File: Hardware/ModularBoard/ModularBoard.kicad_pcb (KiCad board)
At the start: 2 copper layers, 25.4 x 68.6 mm, 16 parts, among them IC1 WS2811-5050, IC2 WS2811-5050, IC3 WS2811-5050, IC4 WS2811-5050, IC5 ATTINY85-P, J1 GSG-USB-MICRO-B, K1 CONN_3, K2 CONN_3, K3 CONN_3, K4 CONN_3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

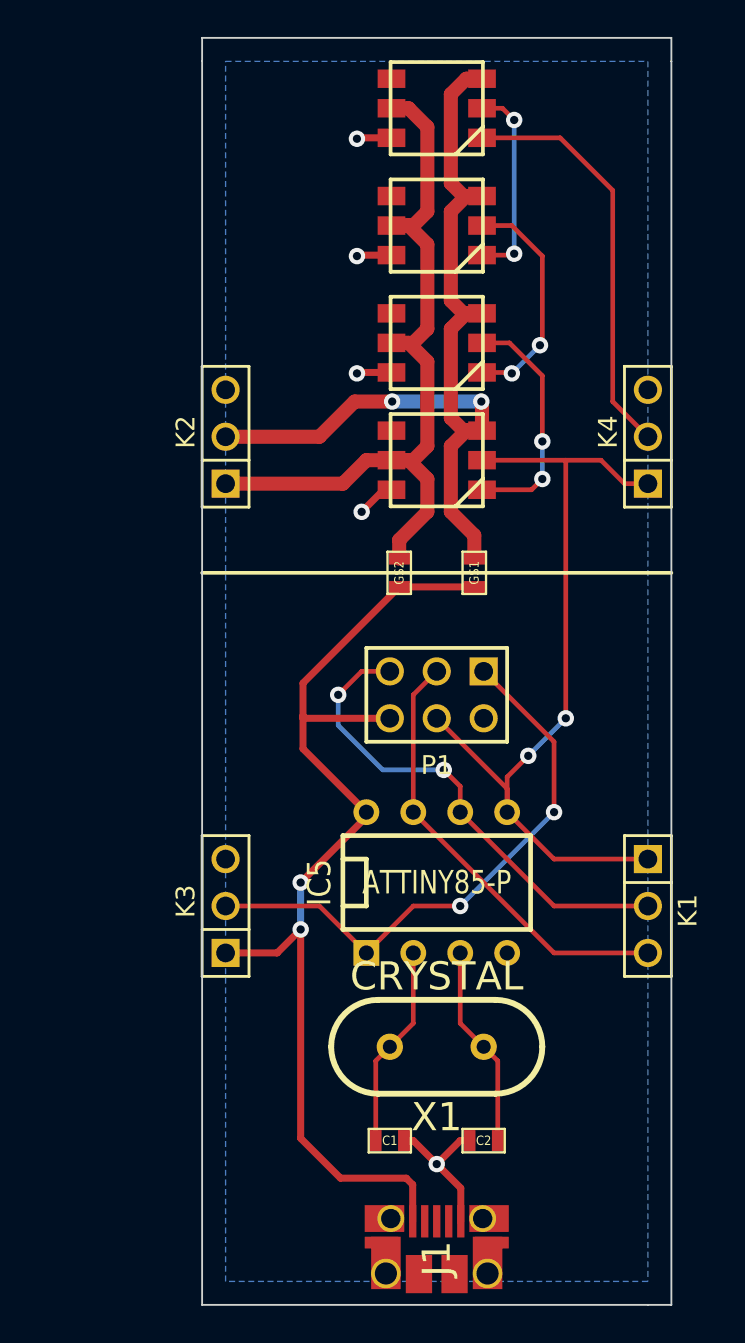
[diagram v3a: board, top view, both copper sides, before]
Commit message: Made the board more compact, might do more by putting ICSP and USB side by side
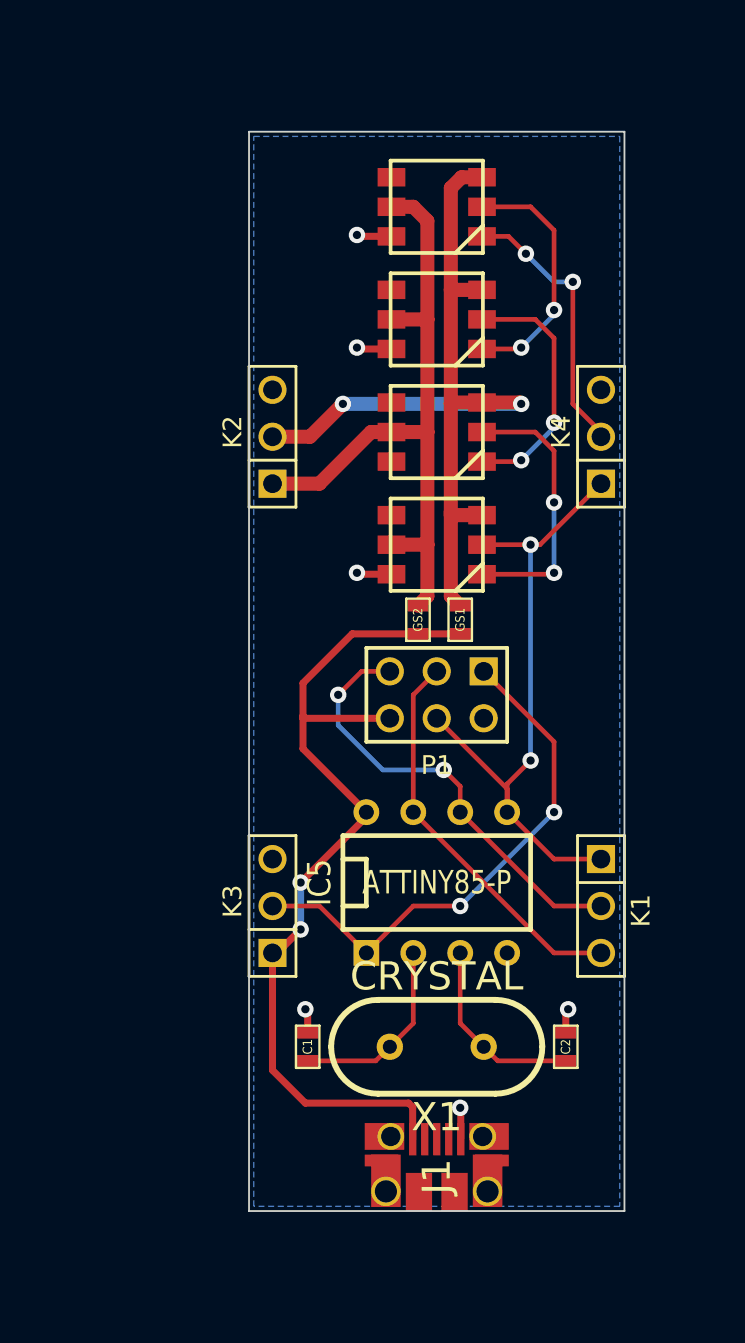
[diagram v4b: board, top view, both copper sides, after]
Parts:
- moved C1 6.75 mm to (219.1, 158.8), turned to 90 degrees
- moved C2 6.75 mm to (233.0, 158.8), turned to 90 degrees
- moved IC4 5.33 mm to (226.1, 113.3)
- moved IC3 5.08 mm to (226.1, 119.4)
- moved IC2 4.83 mm to (226.1, 125.5)
- moved IC1 4.57 mm to (226.1, 131.6)
- moved J1 4.44 mm to (226.1, 168.3)
- moved GS2 2.74 mm to (225.0, 135.6)
- moved GS1 2.65 mm to (227.3, 135.6)
- moved K1 2.54 mm to (234.9, 151.1)
- moved K4 2.54 mm to (234.9, 125.7)
- moved K2 2.54 mm to (217.2, 125.7)
- moved K3 2.54 mm to (217.2, 151.1)
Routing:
- net /MOSI: track 45.2 -> 35.6 mm
- net +5V: track 57.5 -> 49.0 mm
- net VDD: track 44.4 -> 36.7 mm
- net /DO: track 22.4 -> 14.9 mm, vias 0 -> 2
- net GND: track 16.0 -> 10.1 mm, vias 5 -> 6
- net VCC: track 51.4 -> 46.4 mm
- net N-0000013: track 11.0 -> 13.7 mm
- net /MISO: track 26.6 -> 24.1 mm
- net /SCK: track 24.0 -> 21.5 mm
- net /RESET: track 31.2 -> 28.6 mm
- net N-000002: track 13.1 -> 14.9 mm
- net N-0000012: track 12.6 -> 13.8 mm
- net N-0000018: track 11.0 -> 10.4 mm
- net N-0000017: track 11.0 -> 10.4 mm
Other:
- board size 25.4 x 68.6 mm -> 20.3 x 58.4 mm

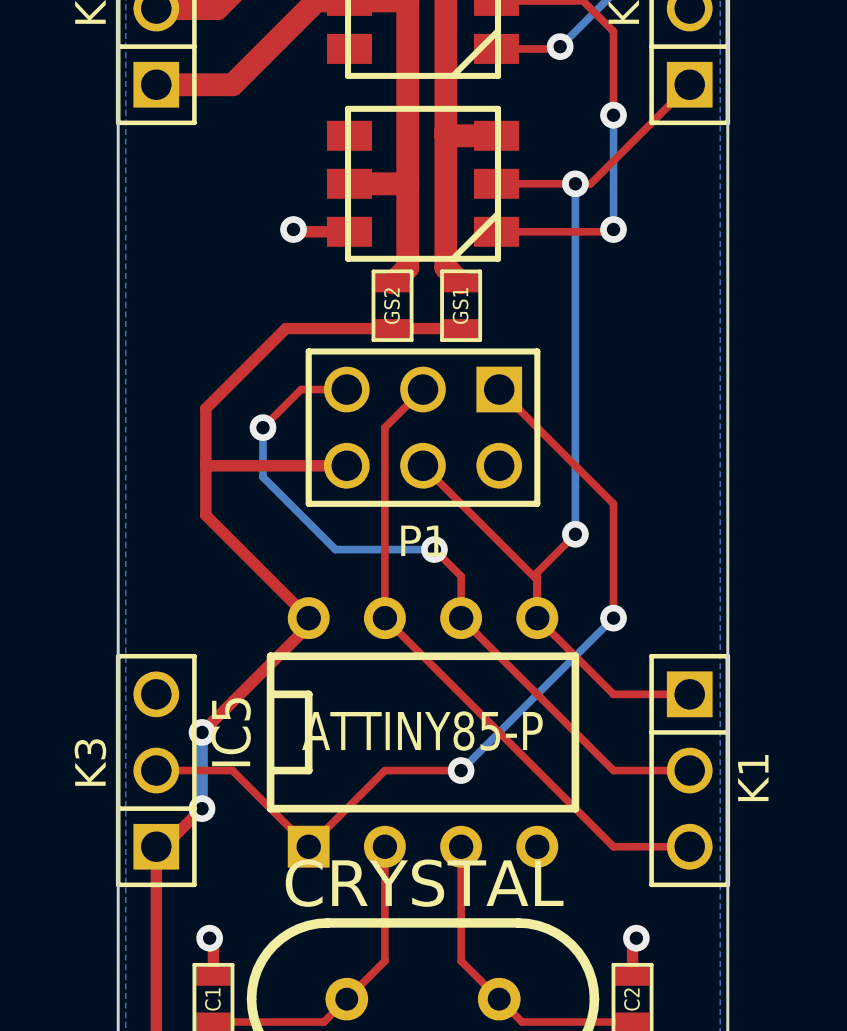
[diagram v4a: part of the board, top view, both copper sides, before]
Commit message: Fixed ICSP header
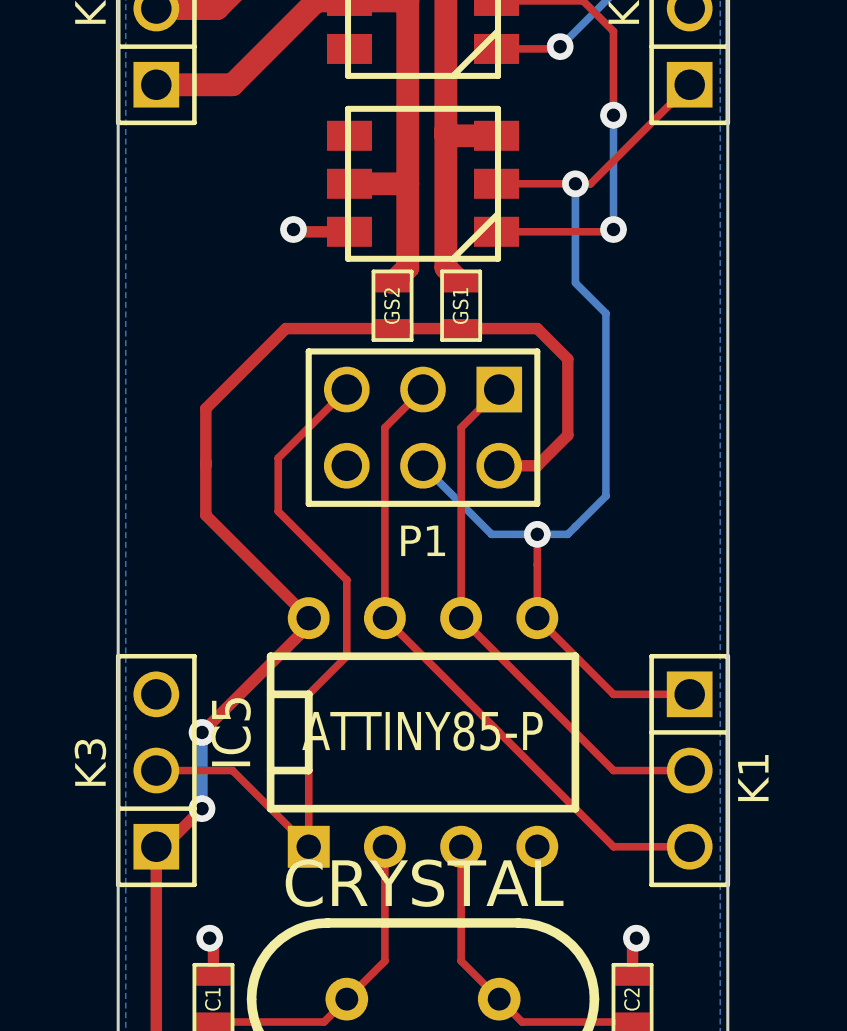
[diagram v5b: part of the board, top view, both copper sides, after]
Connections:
- P1 pad 1: /RESET -> /MISO
- P1 pad 2: GND -> +5V
- P1 pad 5: /MISO -> /RESET
- P1 pad 6: +5V -> GND
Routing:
- net /MISO: track 24.1 -> 17.9 mm, vias 2 -> 0
- net /RESET: track 28.6 -> 23.8 mm, vias 2 -> 0
- net +5V: track 49.0 -> 53.5 mm

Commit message: Its compact! Fits in 5x5cm square
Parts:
- moved P1 25.6 mm to (232.9, 164.3)
- moved K4 15.5 mm to (237.5, 141.0)
- moved K2 15.2 mm to (217.2, 141.0)
- moved GS1 10.5 mm to (228.6, 146.1)
- moved GS2 10.5 mm to (226.3, 146.1)
- moved IC1 9.99 mm to (227.3, 141.5)
- moved IC2 9.99 mm to (227.3, 135.4)
- moved IC3 9.99 mm to (227.3, 129.3)
- moved IC4 9.99 mm to (227.3, 123.2)
- moved C2 9.37 mm to (224.0, 161.3), turned to 0 degrees
- moved C1 7.67 mm to (218.2, 151.1), turned to 180 degrees
- moved IC5 7.58 mm to (230.9, 155.7), turned to 270 degrees
- moved K1 5.68 mm to (237.5, 156.2)
- moved X1 5.49 mm to (223.0, 154.2), turned to 90 degrees
- moved K3 5.08 mm to (217.2, 156.2)
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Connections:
- K1 pad 1: /MOSI -> /SCK
- K1 pad 3: /SCK -> /MOSI
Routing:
- net GND: track 10.1 -> 23.4 mm, vias 6 -> 4
- net /RESET: track 23.8 -> 32.5 mm, vias 0 -> 1
- net /SCK: track 21.5 -> 13.3 mm
- net /MISO: track 17.9 -> 10.9 mm, vias 0 -> 1
- net /MOSI: track 35.1 -> 40.9 mm, vias 2 -> 0
- net /DO: track 14.9 -> 20.1 mm
- net +5V: track 53.5 -> 56.5 mm, vias 2 -> 3
- net N-0000018: track 10.4 -> 8.85 mm
- net N-000005: track 14.9 -> 13.8 mm
- net VCC: track 46.4 -> 47.5 mm
- net N-0000017: track 10.4 -> 9.50 mm
- net VDD: track 36.7 -> 37.5 mm
- net N-0000011: track 13.8 -> 13.2 mm
- net N-0000012: track 13.7 -> 13.2 mm
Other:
- board size 20.3 x 58.4 mm -> 22.9 x 48.3 mm

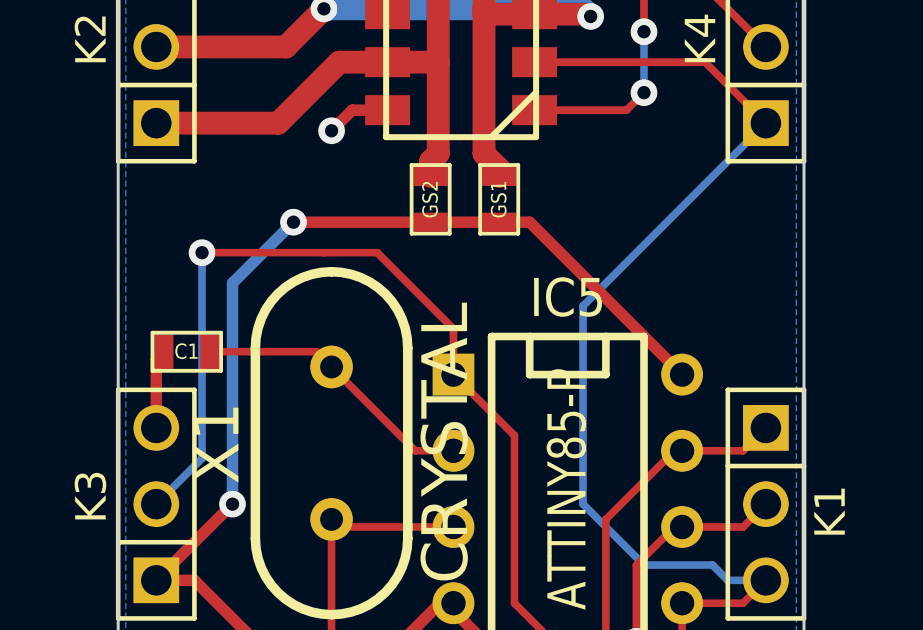
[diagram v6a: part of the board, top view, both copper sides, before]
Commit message: made sure ground was all connected
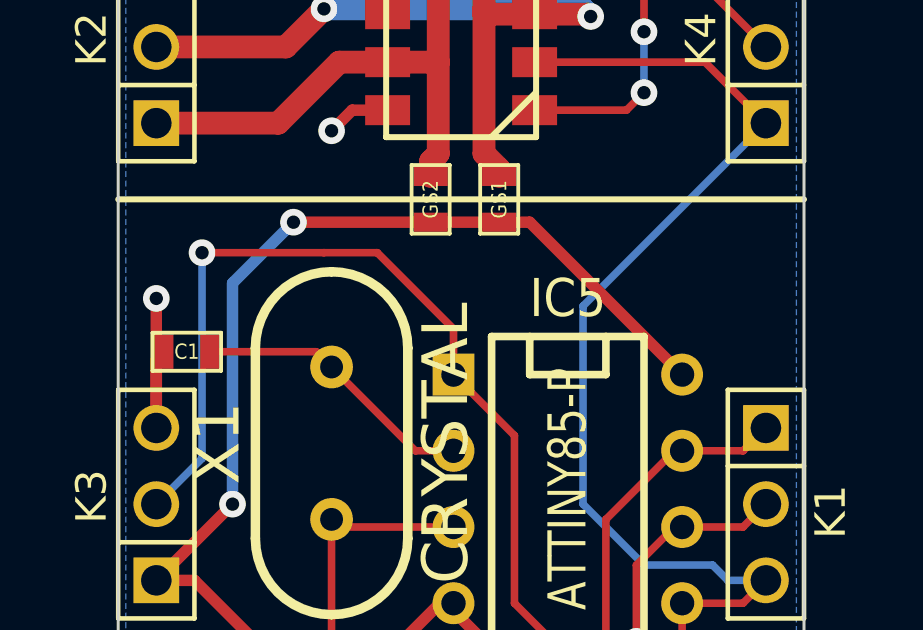
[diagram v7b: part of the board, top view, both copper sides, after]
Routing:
- net GND: track 23.4 -> 27.7 mm, vias 4 -> 5
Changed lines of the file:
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@@
   (general
     (links 43)
-    (no_connects 6)
+    (no_connects 0)
     (area 214.1728 107.42929 237.9472 178.88204)
     (thickness 1.6)
     (drawings 5)
-    (tracks 157)
+    (tracks 159)
     (zones 0)
     (modules 16)
@@
     )
   )
+  (gr_line (start 238.76 146.05) (end 215.9 146.05) (angle 90) (layer F.SilkS) (width 0.2))
   (gr_line (start 215.9 167.64) (end 215.9 119.38) (angle 90) (layer Edge.Cuts) (width 0.1))
   (gr_line (start 238.76 119.38) (end 238.76 167.64) (angle 90) (layer Edge.Cuts) (width 0.1))
   (gr_line (start 215.9 119.38) (end 238.76 119.38) (angle 90) (layer Edge.Cuts) (width 0.1))
   (gr_line (start 238.76 167.64) (end 215.9 167.64) (angle 90) (layer Edge.Cuts) (width 0.1))
-  (dimension 49.784 (width 0.3) (layer F.SilkS)
-    (gr_text "49.784 mm" (at 247.222 142.748 90) (layer F.SilkS)
-      (effects (font (size 1.5 1.5) (thickness 0.3)))
-    )
-    (feature1 (pts (xy 239.522 117.856) (xy 248.572 117.856)))
-    (feature2 (pts (xy 239.522 167.64) (xy 248.572 167.64)))
-    (crossbar (pts (xy 245.872 167.64) (xy 245.872 117.856)))
-    (arrow1a (pts (xy 245.872 117.856) (xy 246.45842 118.982503)))
-    (arrow1b (pts (xy 245.872 117.856) (xy 245.28558 118.982503)))
-    (arrow2a (pts (xy 245.872 167.64) (xy 246.45842 166.513497)))
-    (arrow2b (pts (xy 245.872 167.64) (xy 245.28558 166.513497)))
-  )
   (segment (start 228.6 146.812) (end 229.616 146.812) (width 0.381) (layer F.Cu) (net 1))
   (segment (start 229.616 146.812) (end 234.696 151.892) (width 0.381) (layer F.Cu) (net 1))
@@
   (segment (start 222.21952 162.52952) (end 220.98 161.29) (width 0.381) (layer F.Cu) (net 1))
   (segment (start 220.98 161.29) (end 218.44 158.75) (width 0.381) (layer F.Cu) (net 1))
-  (segment (start 229.78 124.79) (end 230.962 124.79) (width 0.254) (layer F.Cu) (net 2) (status 400000))
-  (segment (start 234.95 138.43) (end 237.49 140.97) (width 0.254) (layer F.Cu) (net 2) (status 800000))
+  (segment (start 229.78 124.79) (end 230.962 124.79) (width 0.254) (layer F.Cu) (net 2))
+  (segment (start 234.95 138.43) (end 237.49 140.97) (width 0.254) (layer F.Cu) (net 2))
   (segment (start 234.95 131.572) (end 234.95 138.43) (width 0.254) (layer F.Cu) (net 2))
   (segment (start 234.95 128.778) (end 234.95 131.572) (width 0.254) (layer F.Cu) (net 2))
@@
   (segment (start 234.696 156.972) (end 236.728 156.972) (width 0.254) (layer F.Cu) (net 3))
   (segment (start 236.728 156.972) (end 237.49 156.21) (width 0.254) (layer F.Cu) (net 3))
-  (segment (start 229.78 141.478) (end 235.458 141.478) (width 0.254) (layer F.Cu) (net 4) (status 400000))
-  (segment (start 235.458 141.478) (end 237.49 143.51) (width 0.254) (layer F.Cu) (net 4) (status 800000))
-  (segment (start 237.49 158.75) (end 236.22 158.75) (width 0.254) (layer B.Cu) (net 4) (status 400000))
-  (segment (start 231.394 149.606) (end 237.49 143.51) (width 0.254) (layer B.Cu) (net 4) (status 800000))
+  (segment (start 229.78 141.478) (end 235.458 141.478) (width 0.254) (layer F.Cu) (net 4))
+  (segment (start 235.458 141.478) (end 237.49 143.51) (width 0.254) (layer F.Cu) (net 4))
+  (segment (start 237.49 158.75) (end 236.22 158.75) (width 0.254) (layer B.Cu) (net 4))
+  (segment (start 231.394 149.606) (end 237.49 143.51) (width 0.254) (layer B.Cu) (net 4))
   (segment (start 231.394 156.21) (end 231.394 149.606) (width 0.254) (layer B.Cu) (net 4))
   (segment (start 233.426 158.242) (end 231.394 156.21) (width 0.254) (layer B.Cu) (net 4))
@@
   (segment (start 234.696 154.432) (end 236.728 154.432) (width 0.254) (layer F.Cu) (net 6))
   (segment (start 236.728 154.432) (end 237.49 153.67) (width 0.254) (layer F.Cu) (net 6))
-  (segment (start 224.88 124.79) (end 223.19 124.79) (width 0.381) (layer F.Cu) (net 7) (status 400000))
+  (segment (start 217.17 153.67) (end 217.17 149.352) (width 0.381) (layer F.Cu) (net 7) (status 400000))
+  (via (at 217.17 149.352) (size 0.889) (layers F.Cu B.Cu) (net 7))
+  (segment (start 224.88 124.79) (end 223.19 124.79) (width 0.381) (layer F.Cu) (net 7))
   (via (at 223.012 124.968) (size 0.889) (layers F.Cu B.Cu) (net 7))
   (segment (start 223.19 124.79) (end 223.012 124.968) (width 0.381) (layer F.Cu) (net 7))
-  (segment (start 224.88 130.886) (end 223.19 130.886) (width 0.381) (layer F.Cu) (net 7) (status 400000))
+  (segment (start 224.88 130.886) (end 223.19 130.886) (width 0.381) (layer F.Cu) (net 7))
   (via (at 223.012 131.064) (size 0.889) (layers F.Cu B.Cu) (net 7))
   (segment (start 223.19 130.886) (end 223.012 131.064) (width 0.381) (layer F.Cu) (net 7))
-  (segment (start 224.88 136.982) (end 223.19 136.982) (width 0.381) (layer F.Cu) (net 7) (status 400000))
+  (segment (start 224.88 136.982) (end 223.19 136.982) (width 0.381) (layer F.Cu) (net 7))
   (via (at 223.012 137.16) (size 0.889) (layers F.Cu B.Cu) (net 7))
   (segment (start 223.19 136.982) (end 223.012 137.16) (width 0.381) (layer F.Cu) (net 7))
-  (segment (start 224.88 143.078) (end 223.698 143.078) (width 0.381) (layer F.Cu) (net 7) (status 400000))
+  (segment (start 224.88 143.078) (end 223.698 143.078) (width 0.381) (layer F.Cu) (net 7))
   (via (at 223.012 143.764) (size 0.889) (layers F.Cu B.Cu) (net 7))
   (segment (start 223.698 143.078) (end 223.012 143.764) (width 0.381) (layer F.Cu) (net 7))
@@
   (segment (start 231.902 136.906) (end 233.426 135.382) (width 0.254) (layer B.Cu) (net 8))
   (via (at 233.426 135.382) (size 0.889) (layers F.Cu B.Cu) (net 8))
-  (segment (start 229.78 129.286) (end 231.902 129.286) (width 0.254) (layer F.Cu) (net 8) (status 400000))
-  (segment (start 231.826 136.982) (end 229.78 136.982) (width 0.254) (layer F.Cu) (net 8) (status 800000))
+  (segment (start 229.78 129.286) (end 231.902 129.286) (width 0.254) (layer F.Cu) (net 8))
+  (segment (start 231.826 136.982) (end 229.78 136.982) (width 0.254) (layer F.Cu) (net 8))
   (segment (start 233.426 130.81) (end 231.902 129.286) (width 0.254) (layer F.Cu) (net 8))
   (segment (start 233.426 129.286) (end 233.426 124.714) (width 0.254) (layer F.Cu) (net 9))
@@
   (segment (start 231.902 130.81) (end 233.426 129.286) (width 0.254) (layer B.Cu) (net 9))
   (via (at 233.426 129.286) (size 0.889) (layers F.Cu B.Cu) (net 9))
-  (segment (start 229.78 123.19) (end 231.902 123.19) (width 0.254) (layer F.Cu) (net 9) (status 400000))
-  (segment (start 231.826 130.886) (end 229.78 130.886) (width 0.254) (layer F.Cu) (net 9) (status 800000))
+  (segment (start 229.78 123.19) (end 231.902 123.19) (width 0.254) (layer F.Cu) (net 9))
+  (segment (start 231.826 130.886) (end 229.78 130.886) (width 0.254) (layer F.Cu) (net 9))
   (segment (start 233.426 124.714) (end 231.902 123.19) (width 0.254) (layer F.Cu) (net 9))
   (segment (start 218.948 151.13) (end 222.504 151.13) (width 0.254) (layer F.Cu) (net 10))
@@
   (segment (start 223.266 156.972) (end 223.012 156.718) (width 0.254) (layer F.Cu) (net 11))
   (segment (start 231.902 135.382) (end 233.426 136.906) (width 0.254) (layer F.Cu) (net 12))
-  (segment (start 229.78 135.382) (end 231.902 135.382) (width 0.254) (layer F.Cu) (net 12) (status 400000))
-  (segment (start 232.842 143.078) (end 229.78 143.078) (width 0.254) (layer F.Cu) (net 12) (status 800000))
+  (segment (start 229.78 135.382) (end 231.902 135.382) (width 0.254) (layer F.Cu) (net 12))
+  (segment (start 232.842 143.078) (end 229.78 143.078) (width 0.254) (layer F.Cu) (net 12))
   (segment (start 233.426 142.494) (end 232.842 143.078) (width 0.254) (layer F.Cu) (net 12))
   (via (at 233.426 142.494) (size 0.889) (layers F.Cu B.Cu) (net 12))
@@
   (via (at 233.426 140.462) (size 0.889) (layers F.Cu B.Cu) (net 12))
   (segment (start 233.426 136.906) (end 233.426 140.462) (width 0.254) (layer F.Cu) (net 12))
-  (segment (start 229.78 139.878) (end 231.572 139.878) (width 0.762) (layer F.Cu) (net 13) (status 400000))
-  (segment (start 221.488 140.97) (end 217.17 140.97) (width 0.762) (layer F.Cu) (net 13) (status 800000))
+  (segment (start 229.78 139.878) (end 231.572 139.878) (width 0.762) (layer F.Cu) (net 13))
+  (segment (start 221.488 140.97) (end 217.17 140.97) (width 0.762) (layer F.Cu) (net 13))
   (segment (start 222.758 139.7) (end 221.488 140.97) (width 0.762) (layer F.Cu) (net 13))
   (via (at 222.758 139.7) (size 0.889) (layers F.Cu B.Cu) (net 13))
@@
   (segment (start 228.092 127.762) (end 228.092 122.428) (width 0.762) (layer F.Cu) (net 13))
   (segment (start 228.6 145.034) (end 228.092 144.526) (width 0.762) (layer F.Cu) (net 13))
-  (segment (start 224.88 141.478) (end 223.266 141.478) (width 0.762) (layer F.Cu) (net 14) (status 400000))
-  (segment (start 221.234 143.51) (end 217.17 143.51) (width 0.762) (layer F.Cu) (net 14) (status 800000))
+  (segment (start 224.88 141.478) (end 223.266 141.478) (width 0.762) (layer F.Cu) (net 14))
+  (segment (start 221.234 143.51) (end 217.17 143.51) (width 0.762) (layer F.Cu) (net 14))
   (segment (start 223.266 141.478) (end 221.234 143.51) (width 0.762) (layer F.Cu) (net 14))
   (segment (start 224.88 141.478) (end 226.568 141.478) (width 0.762) (layer F.Cu) (net 14))
